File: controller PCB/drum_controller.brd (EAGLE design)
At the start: 122.3 x 123.8 mm, 29 parts, among them IC1 7805T

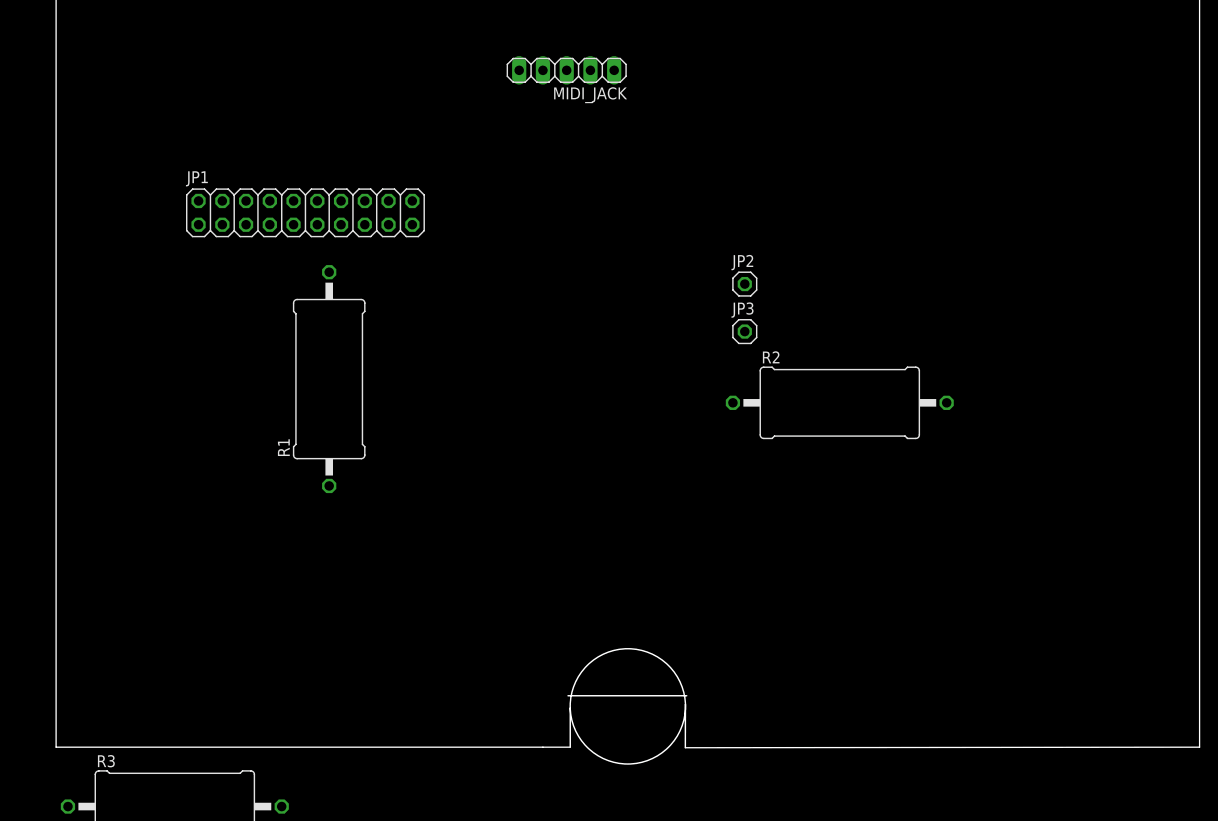
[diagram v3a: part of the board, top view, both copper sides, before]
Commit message: added proper MIDI jack from external library; added lower enclosure notch (will add matching notch with Zoe)
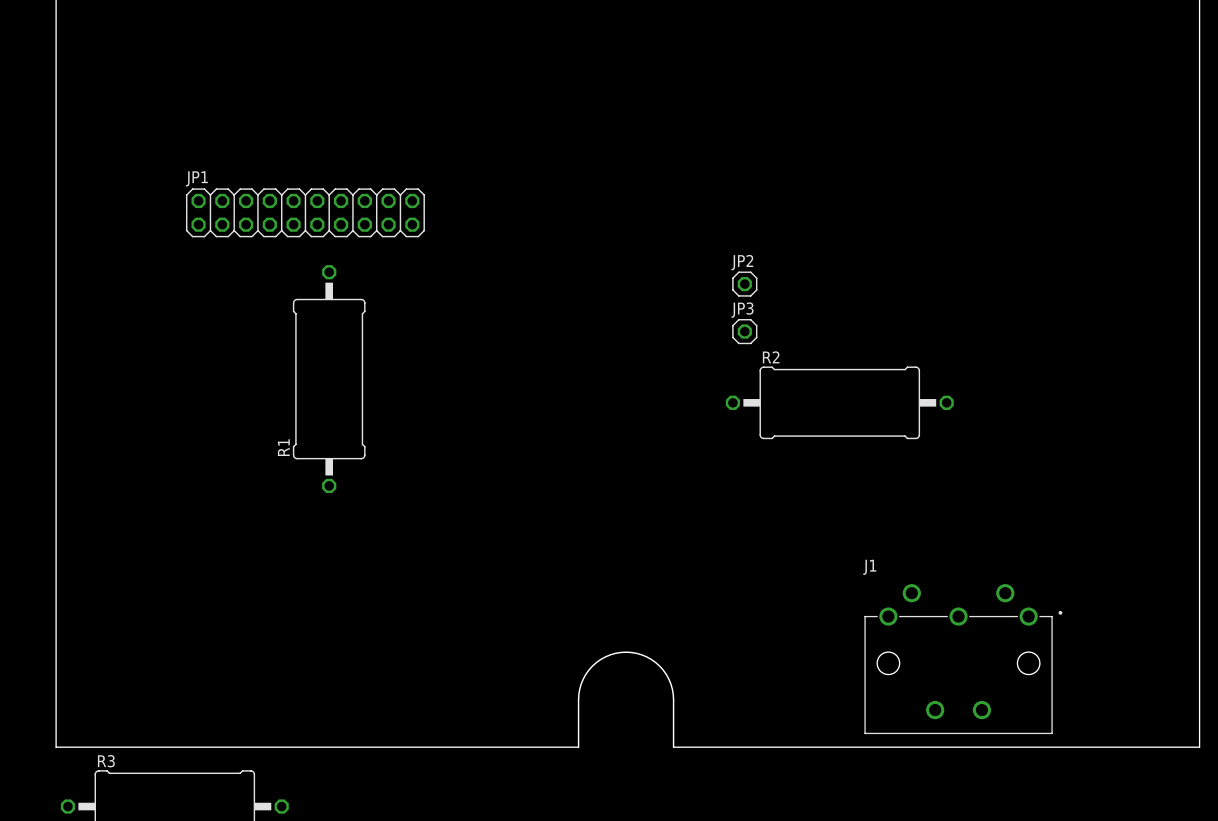
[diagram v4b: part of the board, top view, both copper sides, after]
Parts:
- removed MIDI_JACK: (no value), pinhead:1X05
- added J1: SDS-50J, SDS-50J:CUI_SDS-50J
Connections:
- net GND: now also J1.3; no longer MIDI_JACK.3
- net N$1: now also J1.4; no longer MIDI_JACK.4
- net TXD: now also J1.2; no longer MIDI_JACK.2
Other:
- board size 122.3 x 123.8 mm -> 122.3 x 122 mm
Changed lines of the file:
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@@
 <drawing>
 <settings>
-<setting alwaysvectorfont="yes"/>
+<setting alwaysvectorfont="no"/>
 <setting verticaltext="up"/>
 </settings>
@@
 <board>
 <plain>
-<wire x1="0" y1="0" x2="52.07" y2="0" width="0" layer="20"/>
-<wire x1="52.07" y1="0" x2="54.99" y2="0" width="0" layer="20"/>
-<wire x1="67.3" y1="-0.06" x2="122.3" y2="0" width="0" layer="20"/>
+<wire x1="0" y1="0" x2="55.88" y2="0" width="0" layer="20"/>
+<wire x1="66.04" y1="0" x2="122.3" y2="0" width="0" layer="20"/>
 <wire x1="122.3" y1="0" x2="122.3" y2="122.04" width="0" layer="20"/>
 <wire x1="122.3" y1="122.04" x2="0" y2="122.04" width="0" layer="20"/>
 <wire x1="0" y1="122.04" x2="0" y2="0" width="0" layer="20"/>
-<circle x="61.15" y="4.365" radius="6.165" width="0.1524" layer="20"/>
-<wire x1="67.31" y1="4.58" x2="67.3" y2="-0.06" width="0.1524" layer="20"/>
-<wire x1="54.99" y1="4.18" x2="54.99" y2="0" width="0.1524" layer="20"/>
-<wire x1="54.75" y1="5.5" x2="67.45" y2="5.5" width="0.1524" layer="20"/>
+<wire x1="55.88" y1="0" x2="55.88" y2="5.08" width="0.1524" layer="20"/>
+<wire x1="66.04" y1="0" x2="66.04" y2="5.08" width="0.1524" layer="20"/>
+<wire x1="55.88" y1="5.08" x2="66.04" y2="5.08" width="0.1524" layer="20" curve="-180"/>
 </plain>
 <attributes>
@@
 <elements>
 <element name="JP1" library="pinhead" package="2X10" value="" x="26.67" y="57.15"/>
-<element name="MIDI_JACK" library="pinhead" package="1X05" value="" x="54.61" y="72.39" rot="R180"/>
 <element name="R1" library="rcl" package="P0817/22" value="220" x="29.21" y="39.37" rot="R90"/>
 <element name="JP2" library="pinhead" package="1X01" value="P+" x="73.66" y="49.53"/>
@@
 <element name="JP18" library="pinhead" package="1X02" value="" x="3.81" y="-97.79"/>
 <element name="IC1" library="adafruit" package="TO220H" value="7805T" x="-8.89" y="-86.36"/>
+<element name="J1" library="SDS-50J" package="CUI_SDS-50J" value="SDS-50J" x="96.52" y="13.97">
+<attribute name="MF" value="CUI Inc" x="96.52" y="13.97" size="1.778" layer="27" display="off"/>
+<attribute name="STANDARD" value="Manufacturer recommendations" x="96.52" y="13.97" size="1.778" layer="27" display="off"/>
+</element>
 </elements>
 <signals>
 <signal name="+5V">
 <contactref element="JP1" pad="1"/>
+<contactref element="IC1" pad="3"/>
 <contactref element="R1" pad="2"/>
-<contactref element="IC1" pad="3"/>
 <wire x1="29.21" y1="50.8" x2="-6.35" y2="-96.52" width="0" layer="19" extent="1-1"/>
 <wire x1="15.24" y1="55.88" x2="29.21" y2="50.8" width="0" layer="19" extent="1-1"/>
@@
 <signal name="GND">
 <contactref element="JP1" pad="19"/>
-<contactref element="MIDI_JACK" pad="3"/>
 <contactref element="JP3" pad="1"/>
 <contactref element="R2" pad="1"/>
@@
 <contactref element="JP18" pad="2"/>
 <contactref element="IC1" pad="2"/>
-<wire x1="73.66" y1="44.45" x2="54.61" y2="72.39" width="0" layer="19" extent="1-1"/>
+<contactref element="J1" pad="3"/>
 <wire x1="72.39" y1="36.83" x2="73.66" y2="44.45" width="0" layer="19" extent="1-1"/>
-<wire x1="38.1" y1="55.88" x2="54.61" y2="72.39" width="0" layer="19" extent="1-1"/>
+<wire x1="89.02" y1="13.97" x2="72.39" y2="36.83" width="0" layer="19" extent="1-1"/>
+<wire x1="38.1" y1="55.88" x2="73.66" y2="44.45" width="0" layer="19" extent="1-1"/>
 <wire x1="1.27" y1="-6.35" x2="38.1" y2="55.88" width="0" layer="19" extent="1-1"/>
 <wire x1="6.35" y1="-13.97" x2="1.27" y2="-6.35" width="0" layer="19" extent="1-1"/>
@@
 <wire x1="-8.89" y1="-96.52" x2="5.08" y2="-97.79" width="0" layer="19" extent="1-1"/>
 </signal>
-<signal name="N$1">
-<contactref element="MIDI_JACK" pad="4"/>
-<contactref element="R1" pad="1"/>
-<wire x1="29.21" y1="27.94" x2="52.07" y2="72.39" width="0" layer="19" extent="1-1"/>
-</signal>
 <signal name="TXD">
 <contactref element="JP1" pad="3"/>
-<contactref element="MIDI_JACK" pad="2"/>
-<wire x1="17.78" y1="55.88" x2="57.15" y2="72.39" width="0" layer="19" extent="1-1"/>
+<contactref element="J1" pad="2"/>
+<wire x1="17.78" y1="55.88" x2="96.52" y2="13.97" width="0" layer="19" extent="1-1"/>
 </signal>
 <signal name="A0">
@@
 <wire x1="2.54" y1="-97.79" x2="-11.43" y2="-96.52" width="0" layer="19" extent="1-1"/>
 </signal>
+<signal name="N$1">
+<contactref element="J1" pad="4"/>
+<contactref element="R1" pad="1"/>
+<wire x1="29.21" y1="27.94" x2="101.52" y2="16.47" width="0" layer="19" extent="1-1"/>
+</signal>
 </signals>
